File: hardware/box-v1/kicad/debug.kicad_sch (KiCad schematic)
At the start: 21 parts, among them J501 MCU SWD+UART, J502 MCU USB FS, J503 SoC UART, SW501 RECOVERY, SW502 RESET

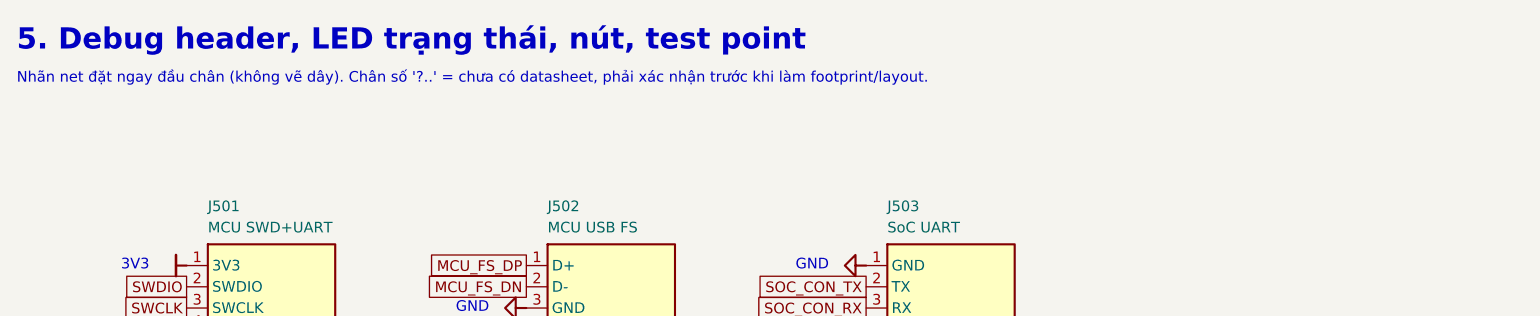
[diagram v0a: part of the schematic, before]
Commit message: hardware/box-v1 in English, with an order package
- Everything in hardware/box-v1 is English: netlist.py, the generators,
  the checks, the README, and the regenerated KiCad sheets, SVGs, BOM
  and netlists. Labels are Confirmed / Likely / Unknown; Option A/B.
- netlist.py carries the ordering data of every BOM line: manufacturer,
  MPN, LCSC code with its evidence, JLCPCB class, price estimate, how it
  is assembled. bom.csv has the new columns; check.py rule R11 checks
  them and the selftest plants 12 faults.
- ORDERING.md: what to send a layout and assembly house, what is done
  and what the vendor does (the layout), the LT7911D documents to ask
  Lontium for, fabrication and assembly specs, bring-up tests, cost
  estimates at 10 and 50 boards, and an RFQ template.
- mechanical.py draws the enclosure outline and connector openings
  (svg/mechanical.svg).
- Design fixes: NRST note (4.7k), the end-of-life inductor replaced
  (SRP1038A-100M), the Bob-Smith capacitor rated 2 kV, capacitor ratings
  matched to stocked parts. Open points are listed in the README.

Co-Authored-By: Claude Opus 5.5 <noreply@anthropic.com>
Claude-Session: https://claude.ai/code/session_01EUDgAy5nU6wYzfaiaKBwjy
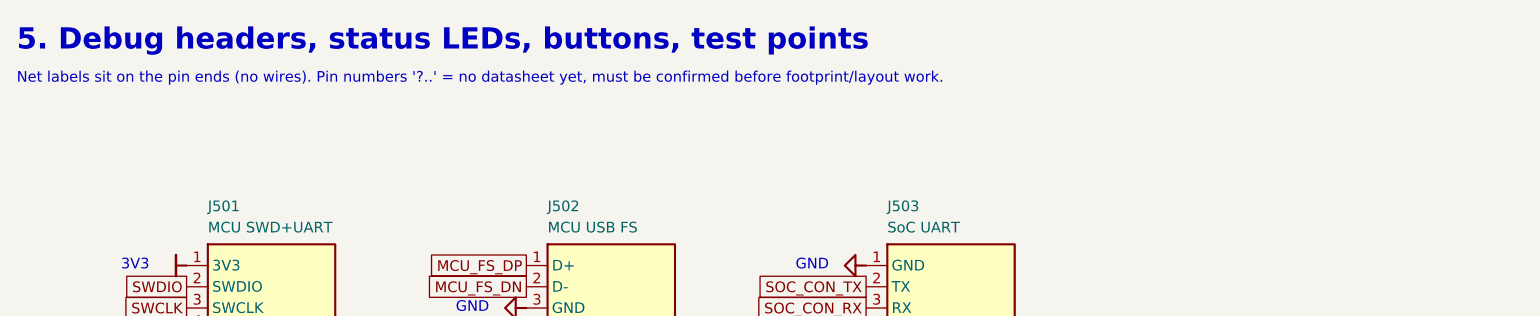
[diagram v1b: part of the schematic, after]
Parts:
- D501: Confidence Chắc -> Confirmed; LCSC (none) -> C2286; MPN LED 0603 red, Vf ≤ 2.2 V -> KT-0603R; Manufacturer (none) -> Hubei KENTO Elec
- D502: Confidence Chắc -> Confirmed; LCSC (none) -> C89811; MPN LED 0603 yellow, Vf ≤ 2.2 V -> NCD0603Y2; Manufacturer (none) -> Foshan NationStar
- D503: Confidence Chắc -> Confirmed; LCSC (none) -> C2289; MPN LED 0603 green, Vf ≤ 2.2 V -> KT-0603YG; Manufacturer (none) -> Hubei KENTO Elec
- J501: Confidence Chắc -> Confirmed; MPN PinHeader 1x07 2.54 -> 61300711121; Manufacturer (none) -> Würth Elektronik
- J502, J503: Confidence Chắc -> Confirmed; MPN PinHeader 1x03 2.54 -> 61300311121; Manufacturer (none) -> Würth Elektronik
- R501, R502: Confidence Chắc -> Confirmed; LCSC (none) -> C25130; MPN (none) -> 0402WGF6800TCE; Manufacturer (none) -> UNI-ROYAL (Uniroyal Elec)
- R503: Confidence Chắc -> Confirmed; MPN (none) -> RC0402FR-07560RL; Manufacturer (none) -> YAGEO
- SW501, SW502: Confidence Chắc -> Confirmed; LCSC (none) -> C2886898; MPN TL3342 -> TL3342F160QG; Manufacturer (none) -> E-Switch
- TP501, TP502, TP503, TP504, TP505, TP506, TP507, TP508, TP509, TP510: Confidence Chắc -> Confirmed; MPN (none) -> none (copper test pad); Manufacturer (none) -> -
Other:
- note added: "5. Debug headers, status LEDs, buttons, test points"
- note added: "Net labels sit on the pin ends (no wires). Pin numbers '?..' = no datasheet yet, must be confirmed before footprint/layout work."
- note removed: "5. Debug header, LED trạng thái, nút, test point"
- note removed: "Nhãn net đặt ngay đầu chân (không vẽ dây). Chân số '?..' = chưa có datasheet, phải xác nhận trước khi làm footprint/layout."
- title: box-v1: debug, LED, nút -> box-v1: debug, LEDs, buttons

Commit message: Box v1: second design review and a PCB generator
- netlist.py: CH224K VBUS pin left open (R102 removed); D101 SMBJ20A clamps
  below the LMR33630's 36 V input; U107 ESD on the rear CC lines; R213 and a
  100 nF C215 on the LT7911D reset; I2C pull-ups on the module's 3.3 V; J201
  HRO TYPE-C-31-M-04 (hybrid, routable B row); TS-1187A buttons; net classes
  shared with the project file and the board.
- placement.py, pcb.py: the 96x66 mm 4-layer board generated from the
  netlist: footprints (custom LT7911D, Core1106, CH224K, vendored HRO
  receptacle), placement, rules, keep-outs, GND fan-out and stitching,
  Freerouting 1.9 round trip, zones, DRC, compact SVG views.
- mechanical.py follows placement.py; README §11, §14, §15 and ORDERING.md
  describe the layout, the review and the remaining LT7911D work; the
  LT7911D datasheet is public on LCSC.

Co-Authored-By: Claude Opus 5.5 <noreply@anthropic.com>
Claude-Session: https://claude.ai/code/session_01EUDgAy5nU6wYzfaiaKBwjy
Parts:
- SW501, SW502: footprint Button_Switch_SMD:SW_SPST_TL3342 -> Button_Switch_SMD:SW_Push_1P1T_XKB_TS-1187A; LCSC C2886898 -> C318884; MPN TL3342F160QG -> TS-1187A-B-A-B; Manufacturer E-Switch -> XKB Connection
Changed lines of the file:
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@@
 		(on_board no)
 		(dnp no)
-		(property "Reference" "#PWR0295"
+		(property "Reference" "#PWR0299"
 			(at 30.48 38.1 0)
 			(effects
@@
 			(project "box-v1"
 				(path "/3958f6c6-dbf7-51be-a7d2-7d63d3ba3dd0/f8f20165-fe63-57ee-90a2-fa6c661a9f9e"
-					(reference "#PWR0295")
+					(reference "#PWR0299")
 					(unit 1)
 				)
@@
 		(on_board no)
 		(dnp no)
-		(property "Reference" "#PWR0296"
+		(property "Reference" "#PWR0300"
 			(at 30.48 45.72 0)
 			(effects
@@
 			(project "box-v1"
 				(path "/3958f6c6-dbf7-51be-a7d2-7d63d3ba3dd0/f8f20165-fe63-57ee-90a2-fa6c661a9f9e"
-					(reference "#PWR0296")
+					(reference "#PWR0300")
 					(unit 1)
 				)
@@
 		(on_board no)
 		(dnp no)
-		(property "Reference" "#PWR0297"
+		(property "Reference" "#PWR0301"
 			(at 71.12 43.18 0)
 			(effects
@@
 			(project "box-v1"
 				(path "/3958f6c6-dbf7-51be-a7d2-7d63d3ba3dd0/f8f20165-fe63-57ee-90a2-fa6c661a9f9e"
-					(reference "#PWR0297")
+					(reference "#PWR0301")
 					(unit 1)
 				)
@@
 		(on_board no)
 		(dnp no)
-		(property "Reference" "#PWR0298"
+		(property "Reference" "#PWR0302"
 			(at 111.76 38.1 0)
 			(effects
@@
 			(project "box-v1"
 				(path "/3958f6c6-dbf7-51be-a7d2-7d63d3ba3dd0/f8f20165-fe63-57ee-90a2-fa6c661a9f9e"
-					(reference "#PWR0298")
+					(reference "#PWR0302")
 					(unit 1)
 				)
@@
 			)
 		)
-		(property "Footprint" "Button_Switch_SMD:SW_SPST_TL3342"
+		(property "Footprint" "Button_Switch_SMD:SW_Push_1P1T_XKB_TS-1187A"
 			(at 38.1 73.66 0)
 			(effects
@@
 			)
 		)
-		(property "MPN" "TL3342F160QG"
+		(property "MPN" "TS-1187A-B-A-B"
 			(at 38.1 73.66 0)
 			(effects
@@
 			)
 		)
-		(property "Manufacturer" "E-Switch"
+		(property "Manufacturer" "XKB Connection"
 			(at 38.1 73.66 0)
 			(effects
@@
 			)
 		)
-		(property "LCSC" "C2886898"
+		(property "LCSC" "C318884"
 			(at 38.1 73.66 0)
 			(effects
@@
 		(on_board no)
 		(dnp no)
-		(property "Reference" "#PWR0299"
+		(property "Reference" "#PWR0303"
 			(at 43.18 73.66 0)
 			(effects
@@
 			(project "box-v1"
 				(path "/3958f6c6-dbf7-51be-a7d2-7d63d3ba3dd0/f8f20165-fe63-57ee-90a2-fa6c661a9f9e"
-					(reference "#PWR0299")
+					(reference "#PWR0303")
 					(unit 1)
 				)
@@
 			)
 		)
-		(property "Footprint" "Button_Switch_SMD:SW_SPST_TL3342"
+		(property "Footprint" "Button_Switch_SMD:SW_Push_1P1T_XKB_TS-1187A"
 			(at 38.1 81.28 0)
 			(effects
@@
 			)
 		)
-		(property "MPN" "TL3342F160QG"
+		(property "MPN" "TS-1187A-B-A-B"
 			(at 38.1 81.28 0)
 			(effects
@@
 			)
 		)
-		(property "Manufacturer" "E-Switch"
+		(property "Manufacturer" "XKB Connection"
 			(at 38.1 81.28 0)
 			(effects
@@
 			)
 		)
-		(property "LCSC" "C2886898"
+		(property "LCSC" "C318884"
 			(at 38.1 81.28 0)
 			(effects
@@
 		(on_board no)
 		(dnp no)
-		(property "Reference" "#PWR0300"
+		(property "Reference" "#PWR0304"
 			(at 43.18 81.28 0)
 			(effects
@@
 			(project "box-v1"
 				(path "/3958f6c6-dbf7-51be-a7d2-7d63d3ba3dd0/f8f20165-fe63-57ee-90a2-fa6c661a9f9e"
-					(reference "#PWR0300")
+					(reference "#PWR0304")
 					(unit 1)
 				)
@@
 		(on_board no)
 		(dnp no)
-		(property "Reference" "#PWR0301"
+		(property "Reference" "#PWR0305"
 			(at 33.02 96.52 0)
 			(effects
@@
 			(project "box-v1"
 				(path "/3958f6c6-dbf7-51be-a7d2-7d63d3ba3dd0/f8f20165-fe63-57ee-90a2-fa6c661a9f9e"
-					(reference "#PWR0301")
+					(reference "#PWR0305")
 					(unit 1)
 				)
@@
 		(on_board no)
 		(dnp no)
-		(property "Reference" "#PWR0302"
+		(property "Reference" "#PWR0306"
 			(at 78.74 81.28 0)
 			(effects
@@
 			(project "box-v1"
 				(path "/3958f6c6-dbf7-51be-a7d2-7d63d3ba3dd0/f8f20165-fe63-57ee-90a2-fa6c661a9f9e"
-					(reference "#PWR0302")
+					(reference "#PWR0306")
 					(unit 1)
 				)
@@
 		(on_board no)
 		(dnp no)
-		(property "Reference" "#PWR0303"
+		(property "Reference" "#PWR0307"
 			(at 78.74 96.52 0)
 			(effects
@@
 			(project "box-v1"
 				(path "/3958f6c6-dbf7-51be-a7d2-7d63d3ba3dd0/f8f20165-fe63-57ee-90a2-fa6c661a9f9e"
-					(reference "#PWR0303")
+					(reference "#PWR0307")
 					(unit 1)
 				)
@@
 		(on_board no)
 		(dnp no)
-		(property "Reference" "#PWR0304"
+		(property "Reference" "#PWR0308"
 			(at 127 73.66 0)
 			(effects
@@
 			(project "box-v1"
 				(path "/3958f6c6-dbf7-51be-a7d2-7d63d3ba3dd0/f8f20165-fe63-57ee-90a2-fa6c661a9f9e"
-					(reference "#PWR0304")
+					(reference "#PWR0308")
 					(unit 1)
 				)
@@
 		(on_board no)
 		(dnp no)
-		(property "Reference" "#PWR0305"
+		(property "Reference" "#PWR0309"
 			(at 127 81.28 0)
 			(effects
@@
 			(project "box-v1"
 				(path "/3958f6c6-dbf7-51be-a7d2-7d63d3ba3dd0/f8f20165-fe63-57ee-90a2-fa6c661a9f9e"
-					(reference "#PWR0305")
+					(reference "#PWR0309")
 					(unit 1)
 				)
@@
 		(on_board no)
 		(dnp no)
-		(property "Reference" "#PWR0306"
+		(property "Reference" "#PWR0310"
 			(at 127 88.9 0)
 			(effects
@@
 			(project "box-v1"
 				(path "/3958f6c6-dbf7-51be-a7d2-7d63d3ba3dd0/f8f20165-fe63-57ee-90a2-fa6c661a9f9e"
-					(reference "#PWR0306")
+					(reference "#PWR0310")
 					(unit 1)
 				)
@@
 		(on_board no)
 		(dnp no)
-		(property "Reference" "#PWR0307"
+		(property "Reference" "#PWR0311"
 			(at 127 96.52 0)
 			(effects
@@
 			(project "box-v1"
 				(path "/3958f6c6-dbf7-51be-a7d2-7d63d3ba3dd0/f8f20165-fe63-57ee-90a2-fa6c661a9f9e"
-					(reference "#PWR0307")
+					(reference "#PWR0311")
 					(unit 1)
 				)
@@
 		(on_board no)
 		(dnp no)
-		(property "Reference" "#PWR0308"
+		(property "Reference" "#PWR0312"
 			(at 172.72 73.66 0)
 			(effects
@@
 			(project "box-v1"
 				(path "/3958f6c6-dbf7-51be-a7d2-7d63d3ba3dd0/f8f20165-fe63-57ee-90a2-fa6c661a9f9e"
-					(reference "#PWR0308")
+					(reference "#PWR0312")
 					(unit 1)
 				)
@@
 		(on_board no)
 		(dnp no)
-		(property "Reference" "#PWR0309"
+		(property "Reference" "#PWR0313"
 			(at 172.72 81.28 0)
 			(effects
@@
 			(project "box-v1"
 				(path "/3958f6c6-dbf7-51be-a7d2-7d63d3ba3dd0/f8f20165-fe63-57ee-90a2-fa6c661a9f9e"
-					(reference "#PWR0309")
+					(reference "#PWR0313")
 					(unit 1)
 				)
@@
 		(on_board no)
 		(dnp no)
-		(property "Reference" "#PWR0310"
+		(property "Reference" "#PWR0314"
 			(at 172.72 88.9 0)
 			(effects
@@
 			(project "box-v1"
 				(path "/3958f6c6-dbf7-51be-a7d2-7d63d3ba3dd0/f8f20165-fe63-57ee-90a2-fa6c661a9f9e"
-					(reference "#PWR0310")
+					(reference "#PWR0314")
 					(unit 1)
 				)
@@
 		(on_board no)
 		(dnp no)
-		(property "Reference" "#PWR0311"
+		(property "Reference" "#PWR0315"
 			(at 172.72 96.52 0)
 			(effects
@@
 			(project "box-v1"
 				(path "/3958f6c6-dbf7-51be-a7d2-7d63d3ba3dd0/f8f20165-fe63-57ee-90a2-fa6c661a9f9e"
-					(reference "#PWR0311")
+					(reference "#PWR0315")
 					(unit 1)
 				)
@@
 		(on_board no)
 		(dnp no)
-		(property "Reference" "#PWR0312"
+		(property "Reference" "#PWR0316"
 			(at 215.9 73.66 0)
 			(effects
@@
 			(project "box-v1"
 				(path "/3958f6c6-dbf7-51be-a7d2-7d63d3ba3dd0/f8f20165-fe63-57ee-90a2-fa6c661a9f9e"
-					(reference "#PWR0312")
+					(reference "#PWR0316")
 					(unit 1)
 				)
@@
 		(on_board no)
 		(dnp no)
-		(property "Reference" "#PWR0313"
+		(property "Reference" "#PWR0317"
 			(at 215.9 81.28 0)
 			(effects
@@
 			(project "box-v1"
 				(path "/3958f6c6-dbf7-51be-a7d2-7d63d3ba3dd0/f8f20165-fe63-57ee-90a2-fa6c661a9f9e"
-					(reference "#PWR0313")
+					(reference "#PWR0317")
 					(unit 1)
 				)
